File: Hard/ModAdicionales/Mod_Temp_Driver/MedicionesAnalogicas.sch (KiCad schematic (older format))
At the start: 28 parts

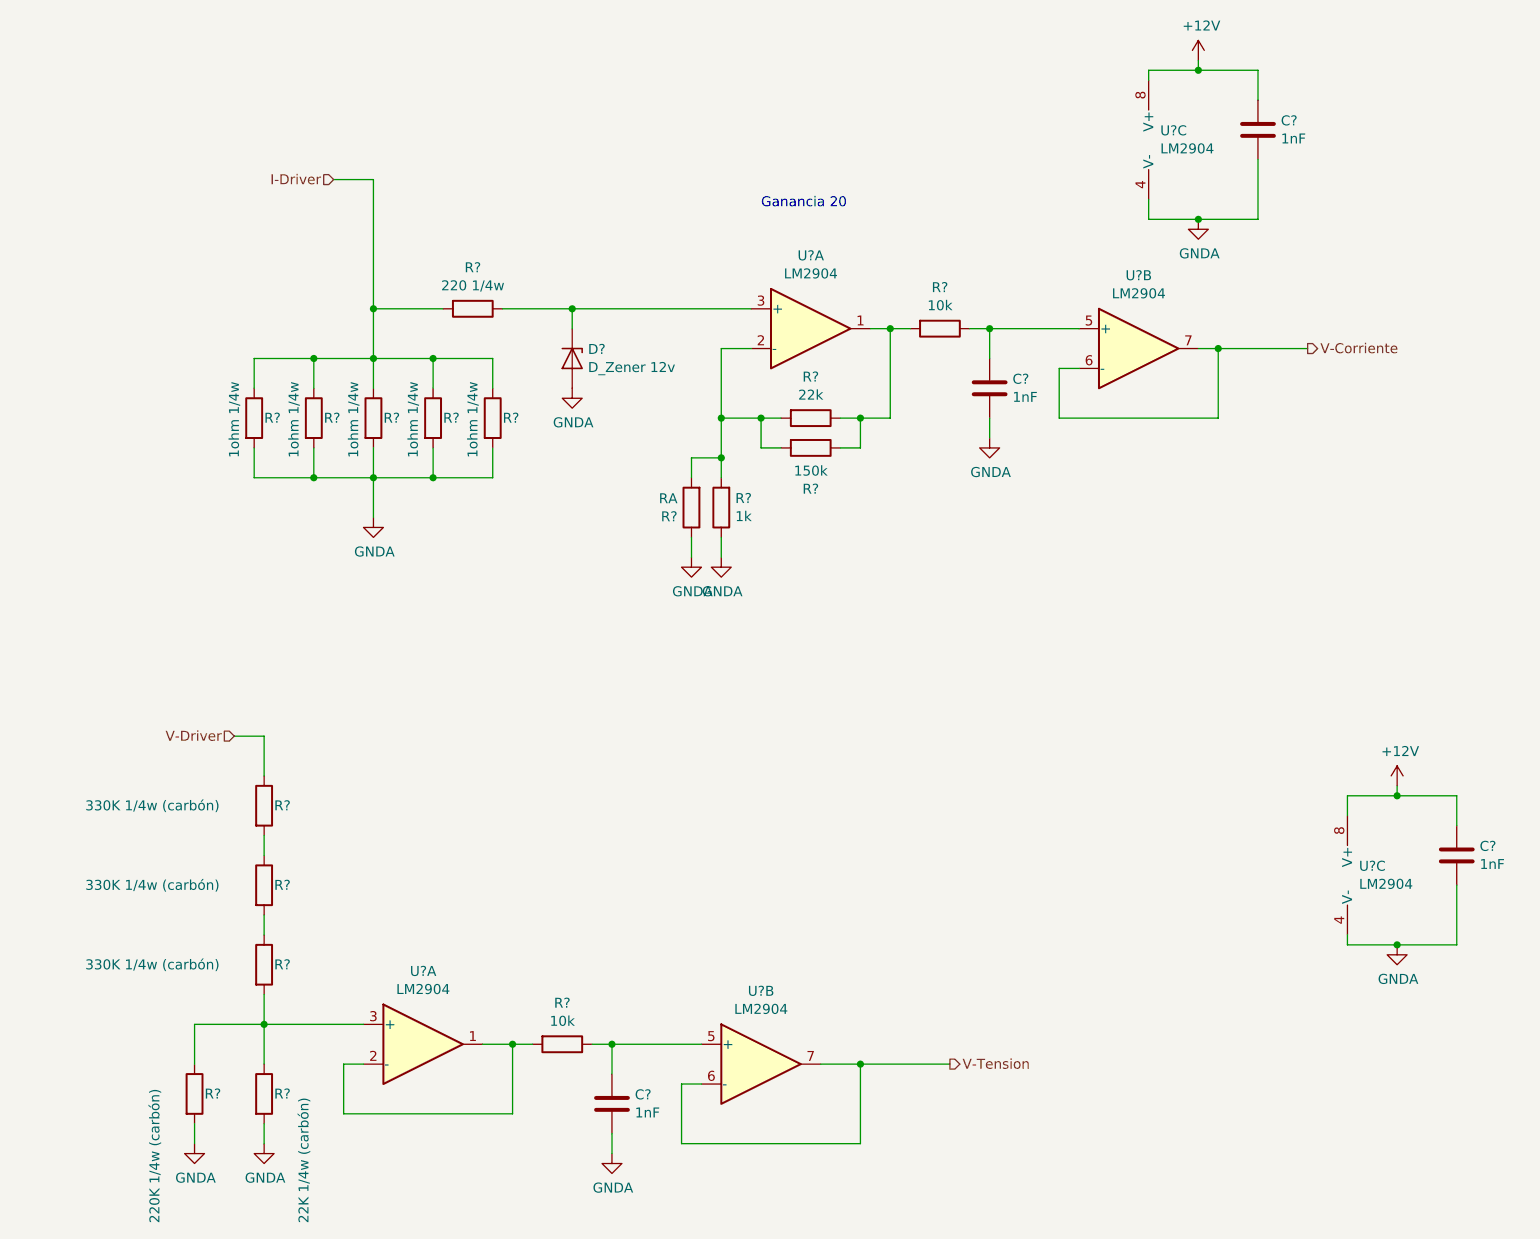
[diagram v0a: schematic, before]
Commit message: Primera correccion en modulos Adicionales y cambio de etapa de salida en modulo principal
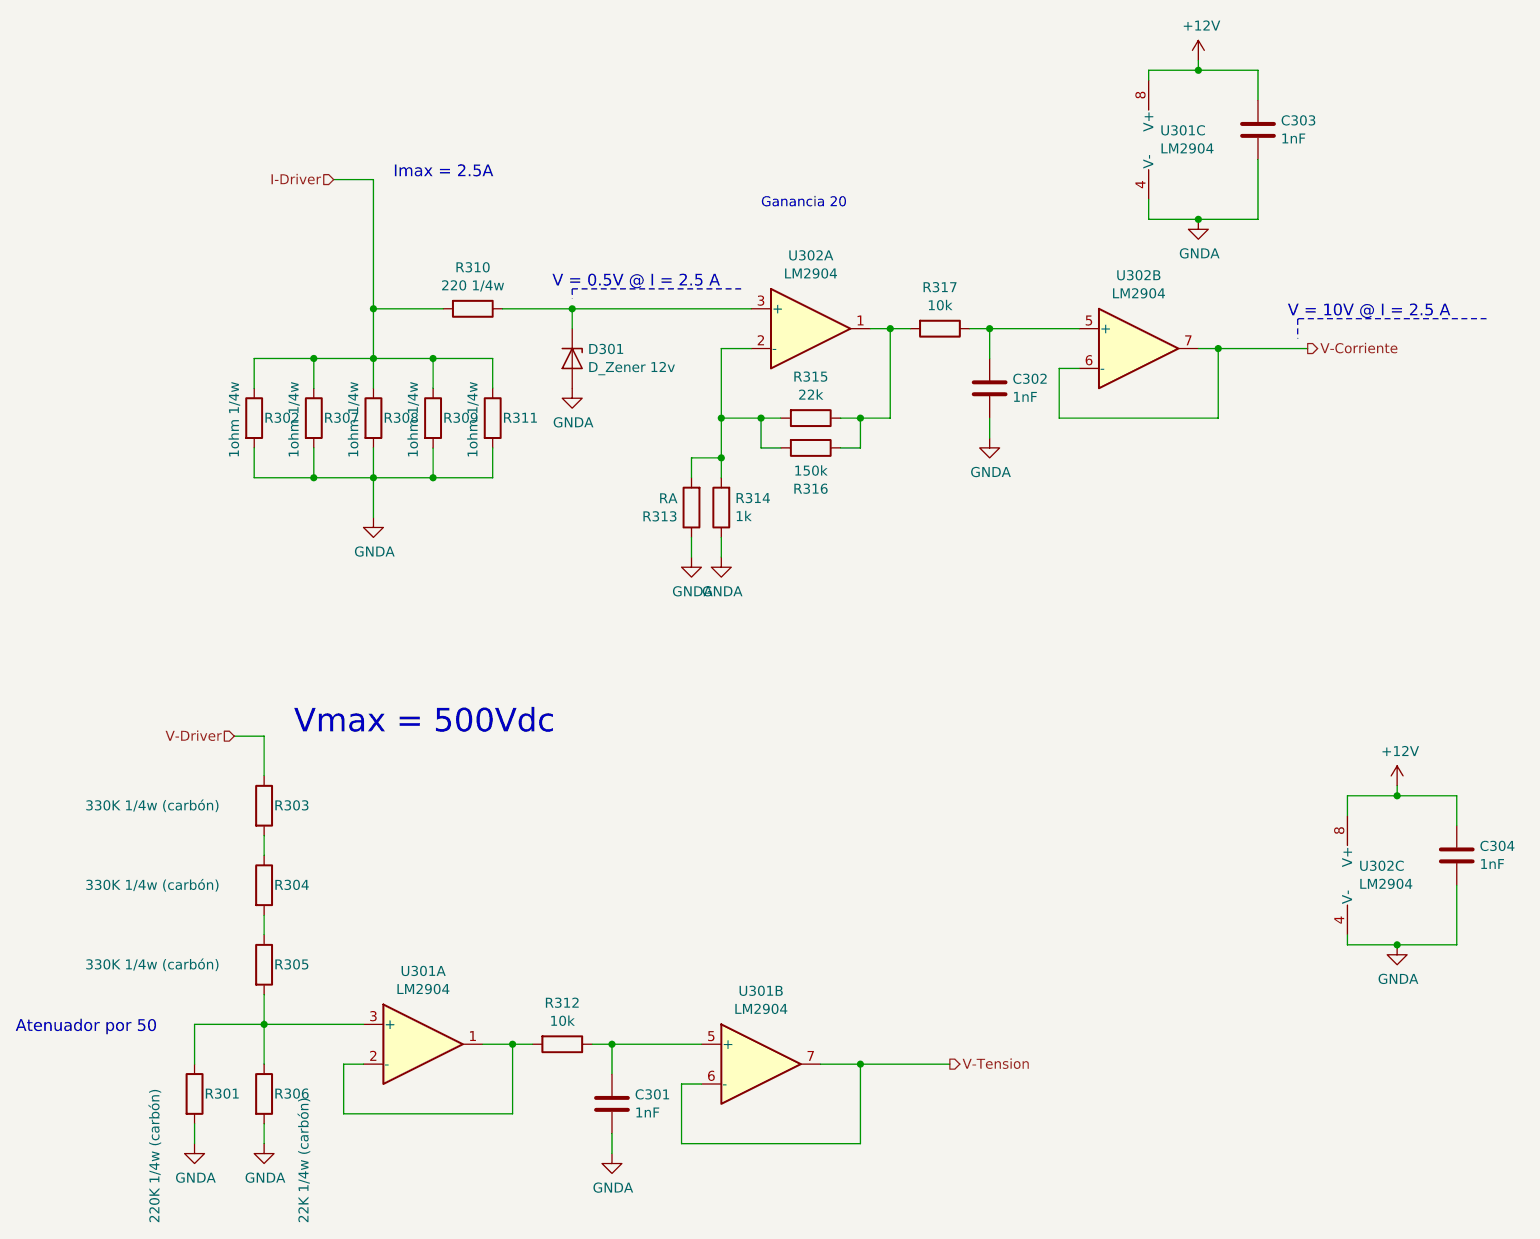
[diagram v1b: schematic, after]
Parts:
- gave numbers to parts that had none: 24
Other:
- note added: "Atenuador por 50"
- note added: "Imax = 2.5A"
- note added: "V = 0.5V @ I = 2.5 A"
- note added: "V = 10V @ I = 2.5 A"
- note added: "Vmax = 500Vdc\n"

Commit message: Asignacion de footprints Modulos adicionales
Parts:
- D301: footprint (none) -> Diode_THT:D_DO-35_SOD27_P7.62mm_Horizontal
- R310: footprint (none) -> Resistor_THT:R_Axial_DIN0309_L9.0mm_D3.2mm_P12.70mm_Horizontal
- U301, U302: footprint (none) -> Package_SO:SO-8_3.9x4.9mm_P1.27mm
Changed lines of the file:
@@
 F 0 "R310" V 3443 2150 50  0000 C CNN
 F 1 "220 1/4w" V 3534 2150 50  0000 C CNN
-F 2 "" V 3580 2150 50  0001 C CNN
+F 2 "Resistor_THT:R_Axial_DIN0309_L9.0mm_D3.2mm_P12.70mm_Horizontal" V 3580 2150 50  0001 C CNN
 F 3 "~" H 3650 2150 50  0001 C CNN
 	1    3650 2150
@@
 F 0 "D301" V 4104 2479 50  0000 L CNN
 F 1 "D_Zener 12v" V 4195 2479 50  0000 L CNN
-F 2 "" H 4150 2400 50  0001 C CNN
+F 2 "Diode_THT:D_DO-35_SOD27_P7.62mm_Horizontal" H 4150 2400 50  0001 C CNN
 F 3 "~" H 4150 2400 50  0001 C CNN
 	1    4150 2400
@@
 F 0 "U302" H 5350 2617 50  0000 C CNN
 F 1 "LM2904" H 5350 2526 50  0000 C CNN
-F 2 "" H 5350 2250 50  0001 C CNN
+F 2 "Package_SO:SO-8_3.9x4.9mm_P1.27mm" H 5350 2250 50  0001 C CNN
 F 3 "http://www.ti.com/lit/ds/symlink/lm358.pdf" H 5350 2250 50  0001 C CNN
 	1    5350 2250
@@
 F 0 "U302" H 7000 2717 50  0000 C CNN
 F 1 "LM2904" H 7000 2626 50  0000 C CNN
-F 2 "" H 7000 2350 50  0001 C CNN
+F 2 "Package_SO:SO-8_3.9x4.9mm_P1.27mm" H 7000 2350 50  0001 C CNN
 F 3 "http://www.ti.com/lit/ds/symlink/lm358.pdf" H 7000 2350 50  0001 C CNN
 	2    7000 2350
@@
 F 0 "U301" H 7108 1346 50  0000 L CNN
 F 1 "LM2904" H 7108 1255 50  0000 L CNN
-F 2 "" H 7150 1300 50  0001 C CNN
+F 2 "Package_SO:SO-8_3.9x4.9mm_P1.27mm" H 7150 1300 50  0001 C CNN
 F 3 "http://www.ti.com/lit/ds/symlink/lm358.pdf" H 7150 1300 50  0001 C CNN
 	3    7150 1300
@@
 F 0 "U301" H 3400 6217 50  0000 C CNN
 F 1 "LM2904" H 3400 6126 50  0000 C CNN
-F 2 "" H 3400 5850 50  0001 C CNN
+F 2 "Package_SO:SO-8_3.9x4.9mm_P1.27mm" H 3400 5850 50  0001 C CNN
 F 3 "http://www.ti.com/lit/ds/symlink/lm358.pdf" H 3400 5850 50  0001 C CNN
 	1    3400 5850
@@
 F 0 "U301" H 5100 6317 50  0000 C CNN
 F 1 "LM2904" H 5100 6226 50  0000 C CNN
-F 2 "" H 5100 5950 50  0001 C CNN
+F 2 "Package_SO:SO-8_3.9x4.9mm_P1.27mm" H 5100 5950 50  0001 C CNN
 F 3 "http://www.ti.com/lit/ds/symlink/lm358.pdf" H 5100 5950 50  0001 C CNN
 	2    5100 5950
@@
 F 0 "U302" H 8108 5046 50  0000 L CNN
 F 1 "LM2904" H 8108 4955 50  0000 L CNN
-F 2 "" H 8150 5000 50  0001 C CNN
+F 2 "Package_SO:SO-8_3.9x4.9mm_P1.27mm" H 8150 5000 50  0001 C CNN
 F 3 "http://www.ti.com/lit/ds/symlink/lm358.pdf" H 8150 5000 50  0001 C CNN
 	3    8150 5000

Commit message: Inicio placement de componentes en Modulos Adicionales
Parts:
- R301: value 220K 1/4w (carbón) -> 220K; footprint Resistor_THT:R_Axial_DIN0309_L9.0mm_D3.2mm_P12.70mm_Horizontal -> Resistor_SMD:R_0805_2012Metric_Pad1.15x1.40mm_HandSolder
- R302, R303, R304, R305, R307, R308, R309, R310, R311: footprint Resistor_THT:R_Axial_DIN0309_L9.0mm_D3.2mm_P12.70mm_Horizontal -> Resistor_THT:R_Axial_DIN0207_L6.3mm_D2.5mm_P7.62mm_Horizontal
- R306: value 22K 1/4w (carbón) -> 22K; footprint Resistor_THT:R_Axial_DIN0309_L9.0mm_D3.2mm_P12.70mm_Horizontal -> Resistor_SMD:R_0805_2012Metric_Pad1.15x1.40mm_HandSolder
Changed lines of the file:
@@
 EESchema Schematic File Version 4
-LIBS:Mod_Temp_Driver-cache
 EELAYER 30 0
 EELAYER END
@@
 F 0 "R302" H 2600 2700 50  0000 L CNN
 F 1 "1ohm 1/4w" V 2450 2500 50  0000 L CNN
-F 2 "Resistor_THT:R_Axial_DIN0309_L9.0mm_D3.2mm_P12.70mm_Horizontal" V 2480 2700 50  0001 C CNN
+F 2 "Resistor_THT:R_Axial_DIN0207_L6.3mm_D2.5mm_P7.62mm_Horizontal" V 2480 2700 50  0001 C CNN
 F 3 "~" H 2550 2700 50  0001 C CNN
 	1    2550 2700
@@
 F 0 "R307" H 2900 2700 50  0000 L CNN
 F 1 "1ohm 1/4w" V 2750 2500 50  0000 L CNN
-F 2 "Resistor_THT:R_Axial_DIN0309_L9.0mm_D3.2mm_P12.70mm_Horizontal" V 2780 2700 50  0001 C CNN
+F 2 "Resistor_THT:R_Axial_DIN0207_L6.3mm_D2.5mm_P7.62mm_Horizontal" V 2780 2700 50  0001 C CNN
 F 3 "~" H 2850 2700 50  0001 C CNN
 	1    2850 2700
@@
 F 0 "R308" H 3200 2700 50  0000 L CNN
 F 1 "1ohm 1/4w" V 3050 2500 50  0000 L CNN
-F 2 "Resistor_THT:R_Axial_DIN0309_L9.0mm_D3.2mm_P12.70mm_Horizontal" V 3080 2700 50  0001 C CNN
+F 2 "Resistor_THT:R_Axial_DIN0207_L6.3mm_D2.5mm_P7.62mm_Horizontal" V 3080 2700 50  0001 C CNN
 F 3 "~" H 3150 2700 50  0001 C CNN
 	1    3150 2700
@@
 F 0 "R309" H 3500 2700 50  0000 L CNN
 F 1 "1ohm 1/4w" V 3350 2500 50  0000 L CNN
-F 2 "Resistor_THT:R_Axial_DIN0309_L9.0mm_D3.2mm_P12.70mm_Horizontal" V 3380 2700 50  0001 C CNN
+F 2 "Resistor_THT:R_Axial_DIN0207_L6.3mm_D2.5mm_P7.62mm_Horizontal" V 3380 2700 50  0001 C CNN
 F 3 "~" H 3450 2700 50  0001 C CNN
 	1    3450 2700
@@
 F 0 "R311" H 3800 2700 50  0000 L CNN
 F 1 "1ohm 1/4w" V 3650 2500 50  0000 L CNN
-F 2 "Resistor_THT:R_Axial_DIN0309_L9.0mm_D3.2mm_P12.70mm_Horizontal" V 3680 2700 50  0001 C CNN
+F 2 "Resistor_THT:R_Axial_DIN0207_L6.3mm_D2.5mm_P7.62mm_Horizontal" V 3680 2700 50  0001 C CNN
 F 3 "~" H 3750 2700 50  0001 C CNN
 	1    3750 2700
@@
 F 0 "R310" V 3443 2150 50  0000 C CNN
 F 1 "220 1/4w" V 3534 2150 50  0000 C CNN
-F 2 "Resistor_THT:R_Axial_DIN0309_L9.0mm_D3.2mm_P12.70mm_Horizontal" V 3580 2150 50  0001 C CNN
+F 2 "Resistor_THT:R_Axial_DIN0207_L6.3mm_D2.5mm_P7.62mm_Horizontal" V 3580 2150 50  0001 C CNN
 F 3 "~" H 3650 2150 50  0001 C CNN
 	1    3650 2150
@@
 F 0 "R305" H 2650 5450 50  0000 L CNN
 F 1 " 330K 1/4w (carbón)" H 1700 5450 50  0000 L CNN
-F 2 "Resistor_THT:R_Axial_DIN0309_L9.0mm_D3.2mm_P12.70mm_Horizontal" V 2530 5450 50  0001 C CNN
+F 2 "Resistor_THT:R_Axial_DIN0207_L6.3mm_D2.5mm_P7.62mm_Horizontal" V 2530 5450 50  0001 C CNN
 F 3 "~" H 2600 5450 50  0001 C CNN
 	1    2600 5450
@@
 F 0 "R304" H 2650 5050 50  0000 L CNN
 F 1 " 330K 1/4w (carbón)" H 1700 5050 50  0000 L CNN
-F 2 "Resistor_THT:R_Axial_DIN0309_L9.0mm_D3.2mm_P12.70mm_Horizontal" V 2530 5050 50  0001 C CNN
+F 2 "Resistor_THT:R_Axial_DIN0207_L6.3mm_D2.5mm_P7.62mm_Horizontal" V 2530 5050 50  0001 C CNN
 F 3 "~" H 2600 5050 50  0001 C CNN
 	1    2600 5050
@@
 F 0 "R303" H 2650 4650 50  0000 L CNN
 F 1 " 330K 1/4w (carbón)" H 1700 4650 50  0000 L CNN
-F 2 "Resistor_THT:R_Axial_DIN0309_L9.0mm_D3.2mm_P12.70mm_Horizontal" V 2530 4650 50  0001 C CNN
+F 2 "Resistor_THT:R_Axial_DIN0207_L6.3mm_D2.5mm_P7.62mm_Horizontal" V 2530 4650 50  0001 C CNN
 F 3 "~" H 2600 4650 50  0001 C CNN
 	1    2600 4650
@@
 AR Path="/5ED5374F/5F0ECABF/5F19BC7D" Ref="R306"  Part="1"
 F 0 "R306" H 2650 6100 50  0000 L CNN
-F 1 "22K 1/4w (carbón)" V 2800 5450 50  0000 L CNN
-F 2 "Resistor_THT:R_Axial_DIN0309_L9.0mm_D3.2mm_P12.70mm_Horizontal" V 2530 6100 50  0001 C CNN
+F 1 "22K " V 2800 5450 50  0000 L CNN
+F 2 "Resistor_SMD:R_0805_2012Metric_Pad1.15x1.40mm_HandSolder" V 2530 6100 50  0001 C CNN
 F 3 "~" H 2600 6100 50  0001 C CNN
 	1    2600 6100
@@
 AR Path="/5ED5374F/5F0ECABF/5F19BC83" Ref="R301"  Part="1"
 F 0 "R301" H 2300 6100 50  0000 L CNN
-F 1 "220K 1/4w (carbón)" V 2050 5450 50  0000 L CNN
-F 2 "Resistor_THT:R_Axial_DIN0309_L9.0mm_D3.2mm_P12.70mm_Horizontal" V 2180 6100 50  0001 C CNN
+F 1 "220K" V 2050 5450 50  0000 L CNN
+F 2 "Resistor_SMD:R_0805_2012Metric_Pad1.15x1.40mm_HandSolder" V 2180 6100 50  0001 C CNN
 F 3 "~" H 2250 6100 50  0001 C CNN
 	1    2250 6100
